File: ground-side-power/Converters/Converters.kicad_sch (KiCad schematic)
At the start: 31 parts, among them J10 Conn_01x03_Female, J12 Conn_01x04_Female, J13 DAQ Voltage Sensing, J14 DAQ Current Sensing, J27 Conn_01x02_Female, U3 K7805-3AR3, U4 INA180, U5 INA180, U6 URB2424LD-20WR3

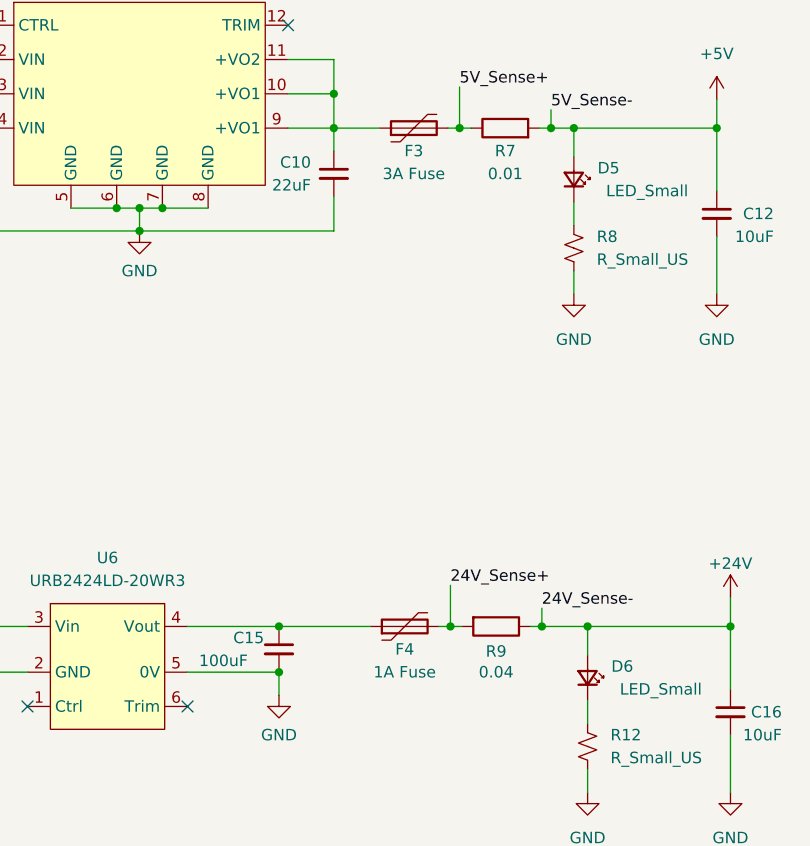
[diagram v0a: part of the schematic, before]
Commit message: Updated Fuses
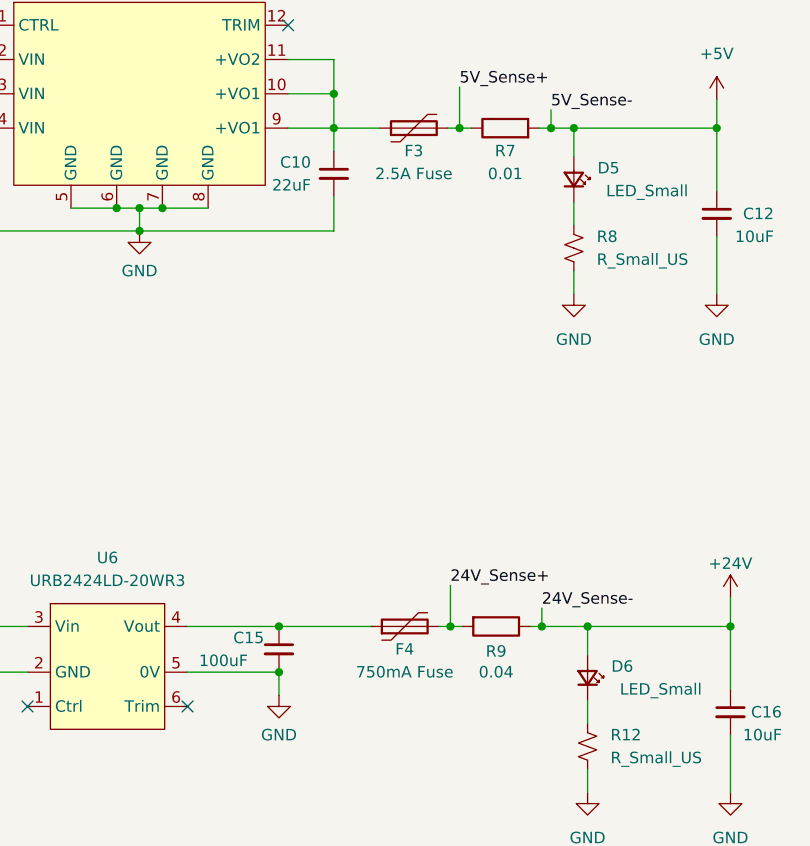
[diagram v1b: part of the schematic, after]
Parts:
- F3: value 3A Fuse -> 2.5A Fuse
- F4: value 1A Fuse -> 750mA Fuse
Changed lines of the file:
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@@
   )
   (text "Shunt Resistor Value Calculations:\nV/I = R\n0.04/Max Current = R"
-    (at 239.776 87.376 180)
+    (at 239.776 87.376 0)
     (effects (font (size 1.27 1.27)) (justify right bottom))
   )
@@
     (in_bom yes) (on_board yes)
     (property "Reference" "F3" (id 0) (at 83.82 50.546 90))
-    (property "Value" "3A Fuse" (id 1) (at 83.82 53.086 90))
+    (property "Value" "2.5A Fuse" (id 1) (at 83.82 53.086 90))
     (property "Footprint" "Fuse:Fuseholder_Clip-6.3x32mm_Littelfuse_102_122_Inline_P34.21x7.62mm_D1.98mm_Horizontal" (id 2) (at 88.9 46.736 0)
       (effects (font (size 1.27 1.27)) (justify left) hide)
@@
     (in_bom yes) (on_board yes)
     (property "Reference" "F4" (id 0) (at 82.804 105.918 90))
-    (property "Value" "1A Fuse" (id 1) (at 82.804 108.458 90))
+    (property "Value" "750mA Fuse" (id 1) (at 82.804 108.458 90))
     (property "Footprint" "Fuse:Fuseholder_Clip-6.3x32mm_Littelfuse_102_122_Inline_P34.21x7.62mm_D1.98mm_Horizontal" (id 2) (at 87.884 102.108 0)
       (effects (font (size 1.27 1.27)) (justify left) hide)
